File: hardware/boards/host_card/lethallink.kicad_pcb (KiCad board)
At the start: 6 copper layers, 121.2 x 98.4 mm, 198 parts, among them J1 PCIe-x4, J2 USB3_Micro_B_Amphenol, J3 Conn_02x05_Odd_Even, J4 Conn_02x04_Odd_Even, J5 Conn_02x04_Odd_Even, J6 SODIMM_260, Q1 Q_NMOS_GSD, Q2 Q_NMOS_GSD, Q3 Q_NMOS_GSD, Q4 Q_NMOS_GSD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

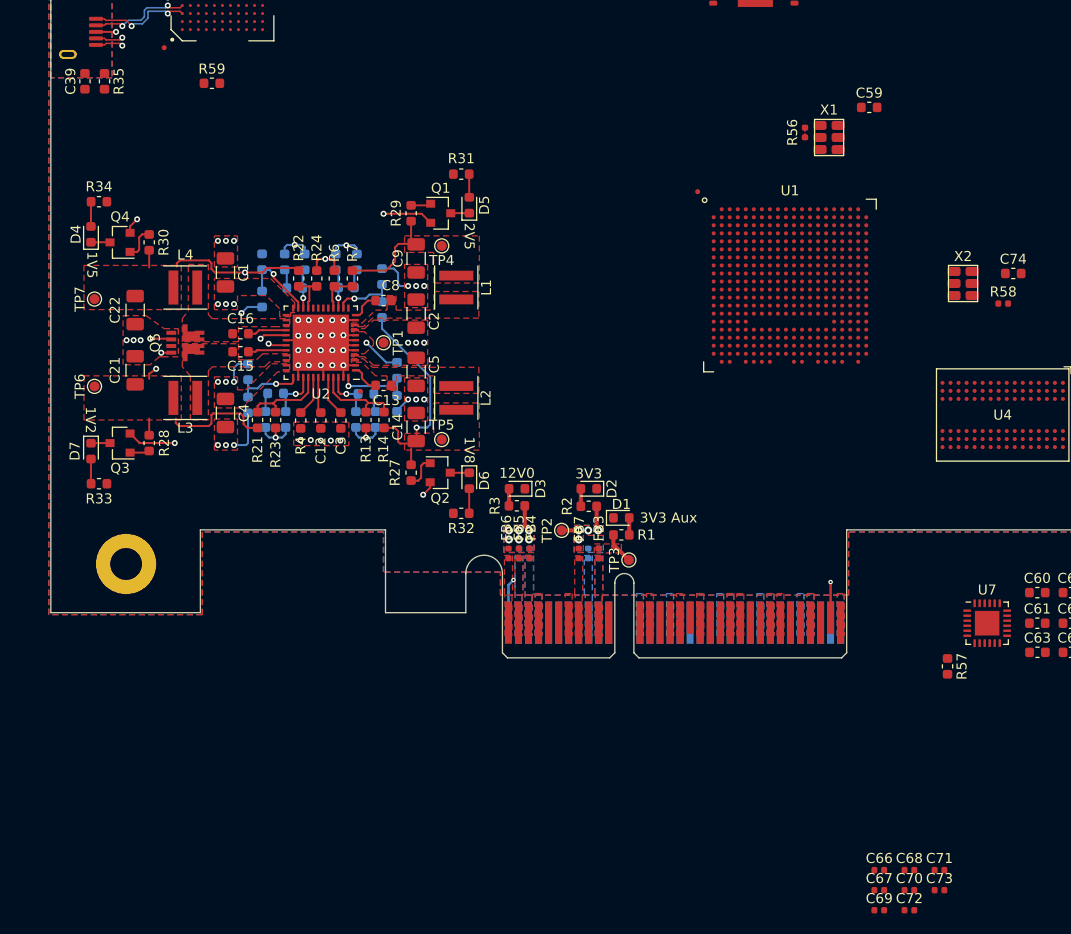
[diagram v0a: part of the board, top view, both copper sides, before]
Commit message: Routed the PCIe TX and RX lines + wiggles, activly routing the clock
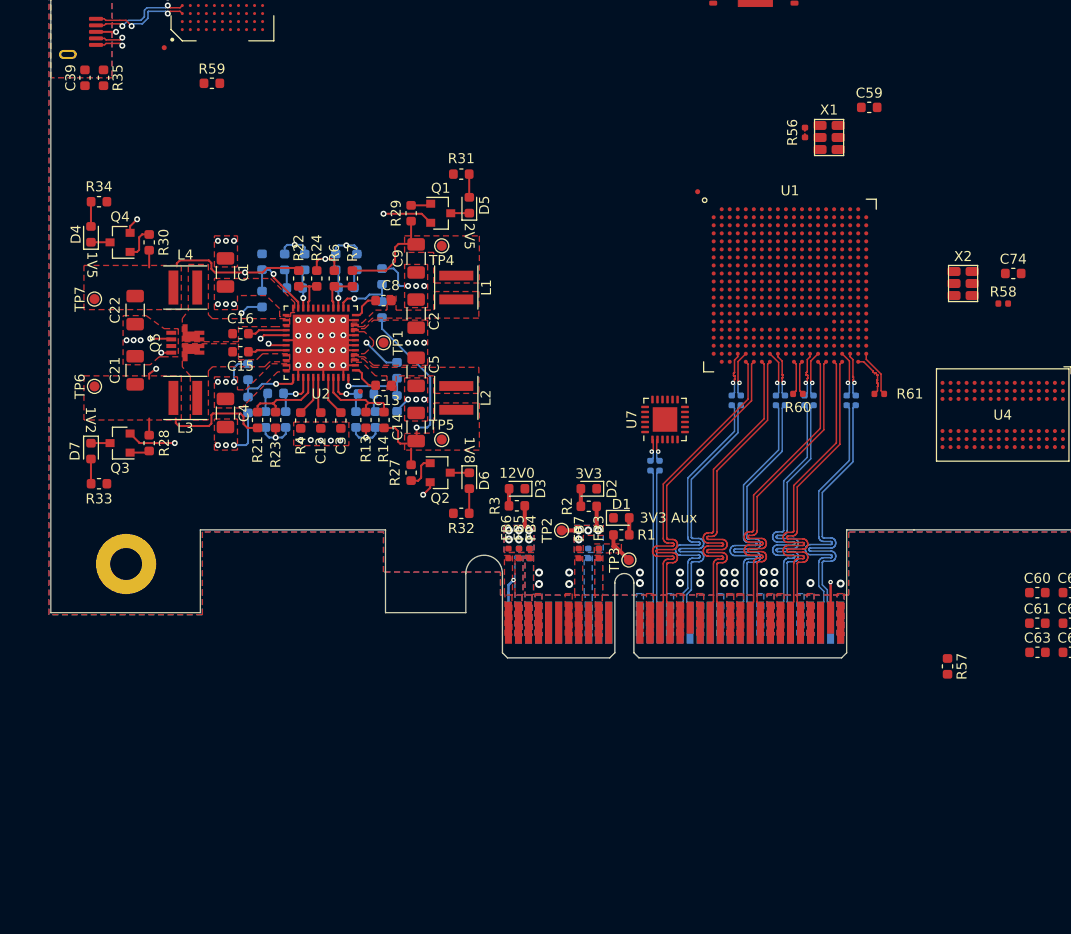
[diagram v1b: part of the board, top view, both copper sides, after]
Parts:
- added C75: 0.1uF, Capacitor_SMD:C_0402_1005Metric, B.Cu at (78.1, 107.7)
- added C76: 0.1uF, Capacitor_SMD:C_0402_1005Metric, B.Cu at (77.2, 107.7)
- added R60: 100, Resistor_SMD:R_0402_1005Metric, F.Cu at (91.9, 100.5)
- added R61: 100, Resistor_SMD:R_0402_1005Metric, F.Cu at (100.0, 100.5)
- C66, C67, C68, C69, C70, C71, C72, C73: value 100nF -> 0.1uF; moved to B.Cu
- moved C73 51.5 mm to (89.7, 101.2), turned to 90 degrees
- moved C69 51.2 mm to (93.5, 101.2), turned to 90 degrees
- moved C72 51.2 mm to (96.8, 101.2), turned to 90 degrees
- moved C68 49.7 mm to (86.2, 101.2), turned to 90 degrees
- moved C67 49.4 mm to (92.5, 101.2), turned to 90 degrees
- moved C71 49.3 mm to (90.6, 101.2), turned to 90 degrees
- moved C70 49.1 mm to (97.7, 101.2), turned to 90 degrees
- moved C66 49.1 mm to (85.3, 101.2), turned to 90 degrees
- moved U7 38.0 mm to (78.7, 103.1), turned to 90 degrees
- moved R35 0.36 mm to (22.7, 69.0)
- moved C39 0.35 mm to (20.9, 69.0)
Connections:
- J1 pad B19: /PCIe Interface/TX1_N -> /PCIe Interface/TX1_P
- U1 pad Y16: /PCIe Interface/TX3_N -> /PCIe Interface/TX3_P
- U1 pad Y17: /PCIe Interface/TX3_P -> /PCIe Interface/TX3_N
- U1 pad Y7: /PCIe Interface/TX1_N -> /PCIe Interface/TX1_P
- U7 pad 1: /PCIe Interface/REFCLK_P -> /PCIe Interface/REFCLK+
- U7 pad 10: Net-(U7-Pad10) -> /PCIe Interface/REFCLK1+
- U7 pad 13: Net-(U7-Pad13) -> /PCIe Interface/REFCLK0-
- U7 pad 14: Net-(U7-Pad14) -> /PCIe Interface/REFCLK0+
- U7 pad 17: /PCIe Interface/REFCLK1- -> Net-(U7-Pad17)
- U7 pad 18: /PCIe Interface/REFCLK1+ -> Net-(U7-Pad18)
- U7 pad 2: /PCIe Interface/REFCLK_N -> /PCIe Interface/REFCLK-
- U7 pad 21: /PCIe Interface/REFCLK0- -> Net-(U7-Pad21)
- U7 pad 22: /PCIe Interface/REFCLK0+ -> Net-(U7-Pad22)
- U7 pad 9: Net-(U7-Pad9) -> /PCIe Interface/REFCLK1-
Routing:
- net /PCIe Interface/TX1_P: track 0.00 -> 35.0 mm
- net /PCIe Interface/TX1_N: track 0.00 -> 35.0 mm
- net /PCIe Interface/TX2_P: track 0.00 -> 35.0 mm
- net /PCIe Interface/TX2_N: track 0.00 -> 35.0 mm
- net /PCIe Interface/TX3_P: track 0.00 -> 35.0 mm
- net /PCIe Interface/TX3_N: track 0.00 -> 35.0 mm
- net /PCIe Interface/TX0_P: track 0.00 -> 35.0 mm
- net /PCIe Interface/TX0_N: track 0.00 -> 35.0 mm
- net /PCIe Interface/RX2_P: track 0.00 -> 30.3 mm
- net /PCIe Interface/RX2_N: track 0.00 -> 30.3 mm
- net /PCIe Interface/RX3_P: track 0.00 -> 30.3 mm
- net /PCIe Interface/RX3_N: track 0.00 -> 30.3 mm
- net /PCIe Interface/RX0_P: track 0.00 -> 30.3 mm
- net /PCIe Interface/RX0_N: track 0.00 -> 30.3 mm
- net /PCIe Interface/RX1_P: track 0.00 -> 30.2 mm
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
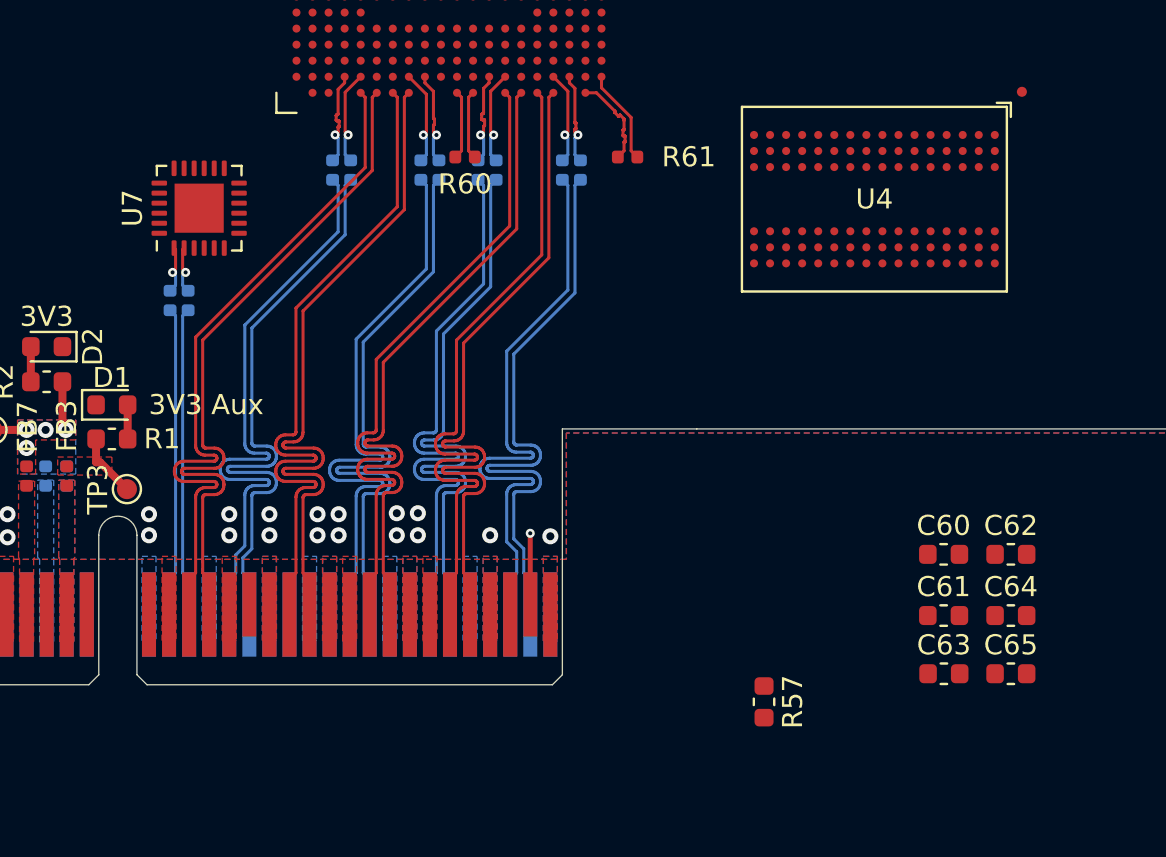
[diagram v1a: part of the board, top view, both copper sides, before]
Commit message: Completed the layout for the PCIe REFCLK buffer and ensured the REFCLK traces were not skewed and that they are wiggled properly
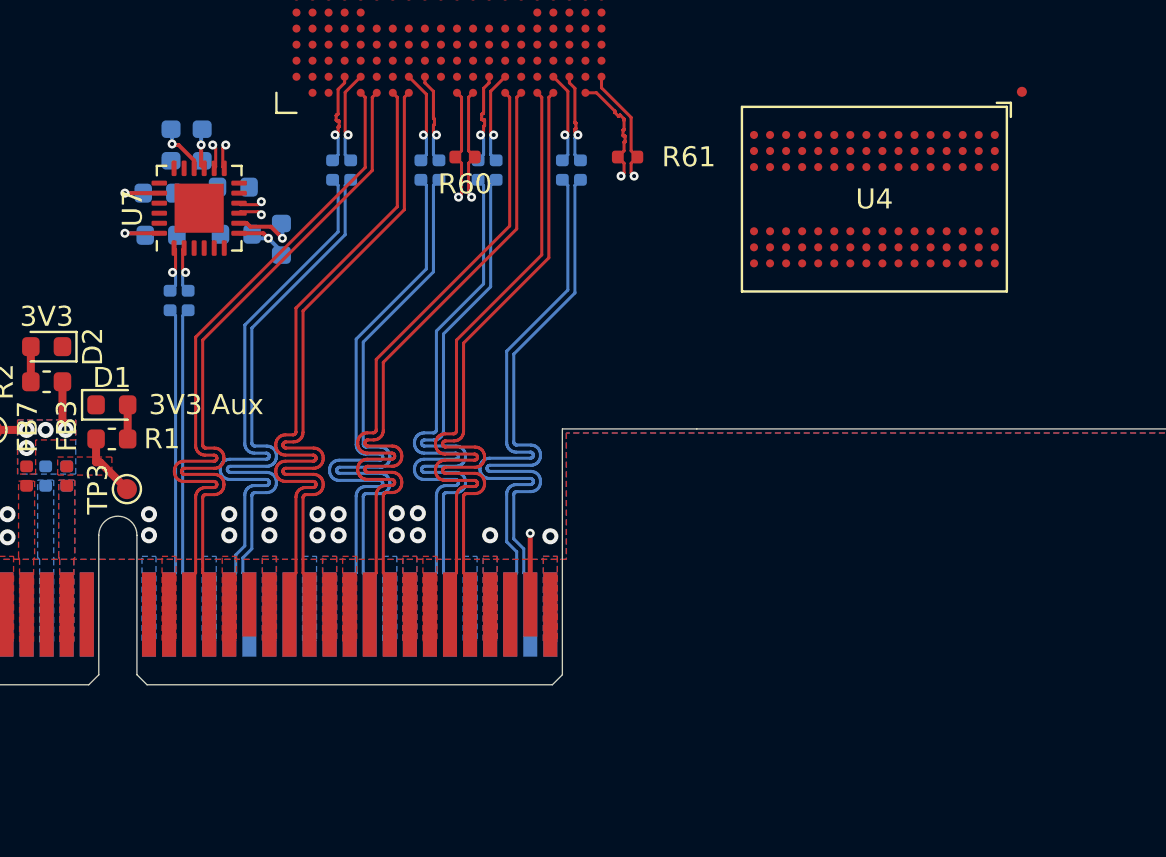
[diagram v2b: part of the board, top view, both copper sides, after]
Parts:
- C60, C61, C62, C63, C64, C65, R57: moved to B.Cu
- moved C65 48.7 mm to (76.7, 102.3), turned to 180 degrees
- moved C63 46.7 mm to (77.2, 100.0), turned to 90 degrees
- moved C64 46.6 mm to (78.8, 100.0), turned to 90 degrees
- moved C61 43.4 mm to (76.8, 104.5)
- moved C62 41.8 mm to (80.5, 104.4)
- moved C60 39.9 mm to (80.3, 102.0), turned to 180 degrees
- moved R57 33.3 mm to (82.8, 104.7)
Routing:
- net /PCIe Interface/REFCLK1+: track 4.72 -> 34.7 mm, vias 0 -> 2
- net /PCIe Interface/REFCLK1-: track 4.74 -> 34.7 mm, vias 0 -> 2
- net /PCIe Interface/REFCLK0+: track 3.42 -> 33.4 mm, vias 0 -> 2
- net /PCIe Interface/REFCLK0-: track 3.42 -> 33.4 mm, vias 0 -> 2
- net +1V8: track 20.0 -> 33.5 mm, vias 1 -> 6
- net Net-(R57-Pad1): track 0.00 -> 3.24 mm, vias 0 -> 1

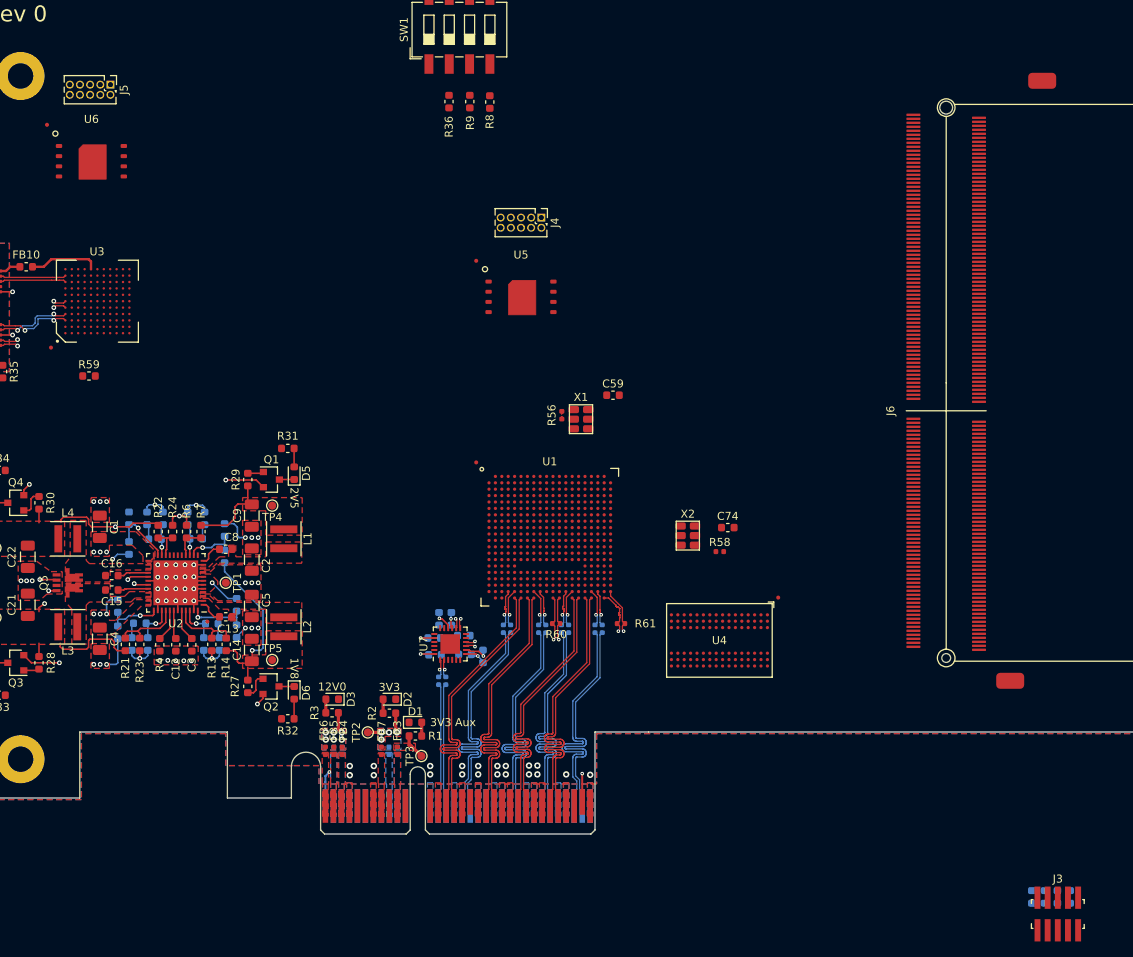
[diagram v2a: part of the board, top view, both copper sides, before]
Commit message: Added a fiducial to for U7. Changed the two pin-headers to the keyd  samtec connectors. Some other misc updates
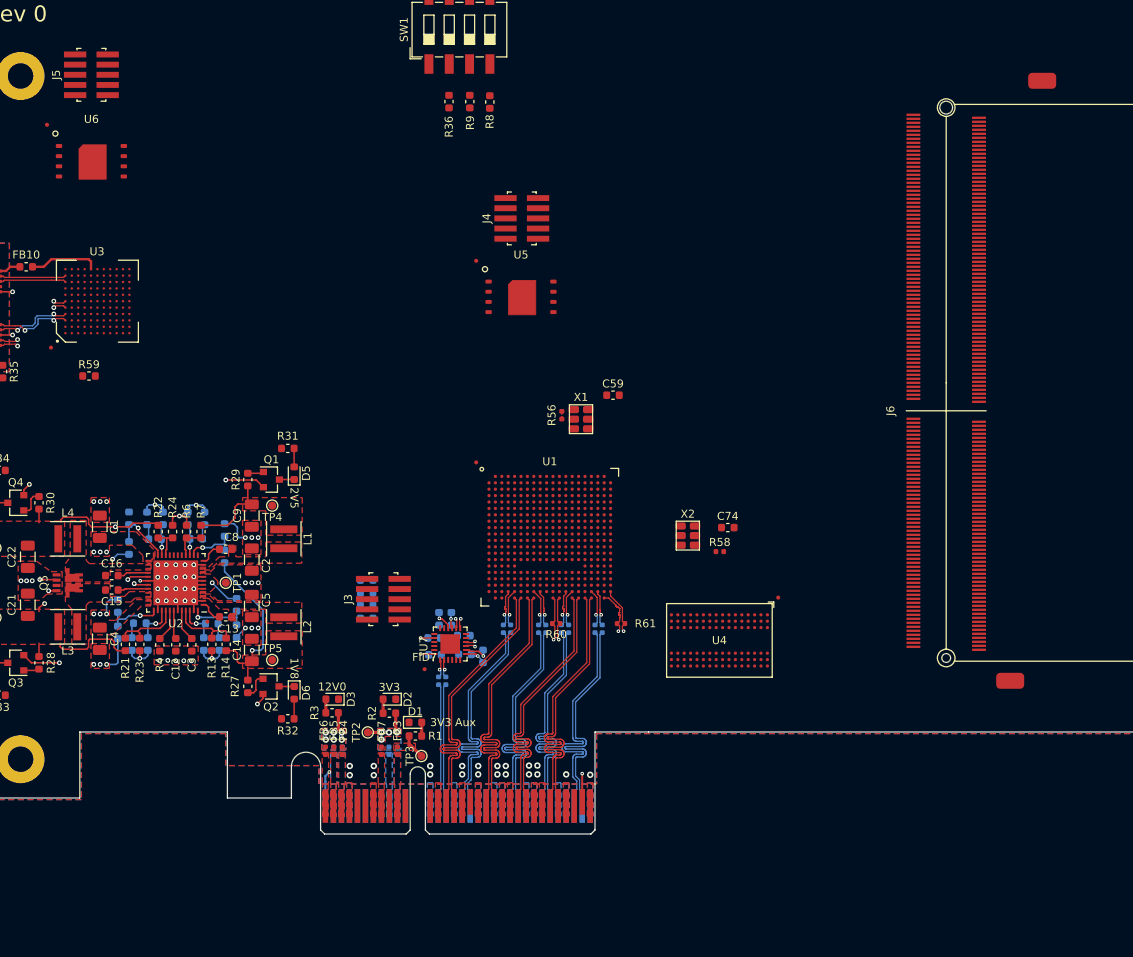
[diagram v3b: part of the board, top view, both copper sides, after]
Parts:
- added FID7: Fiducial, Fiducial:Fiducial_0.5mm_Mask1mm, F.Cu at (75.5, 106.2)
- J4, J5: footprint Connector_PinHeader_1.27mm:PinHeader_2x05_P1.27mm_Vertical -> lethalbit-connectors:FTSH-105-01-L-DV-K-TR
- moved R41 96.4 mm to (68.2, 95.1), turned to 0 degrees
- moved R40 94.3 mm to (68.2, 96.7), turned to 0 degrees
- moved J3 93.0 mm to (70.3, 97.5), turned to 90 degrees
- moved R39 92.2 mm to (68.2, 98.3), turned to 0 degrees
- moved R38 90.1 mm to (68.2, 99.9), turned to 0 degrees
- moved J5 2.68 mm to (33.8, 31.9), turned to 90 degrees
- moved J4 2.44 mm to (87.6, 49.9), turned to 90 degrees
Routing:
- net GND: track 59.5 -> 60.5 mm, vias 71 -> 72

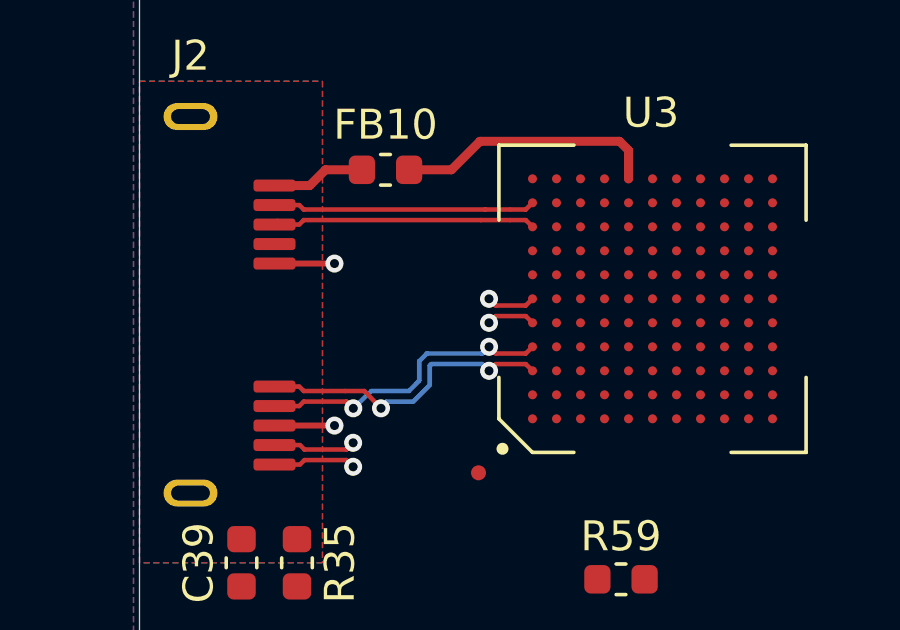
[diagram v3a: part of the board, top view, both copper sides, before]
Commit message: Fixed up the consistancy of value naming, 100nF -> 0.1uF. Added the caps for the USB SSRX lines, moved the Ferrite for VBUS to fix a net naming issue
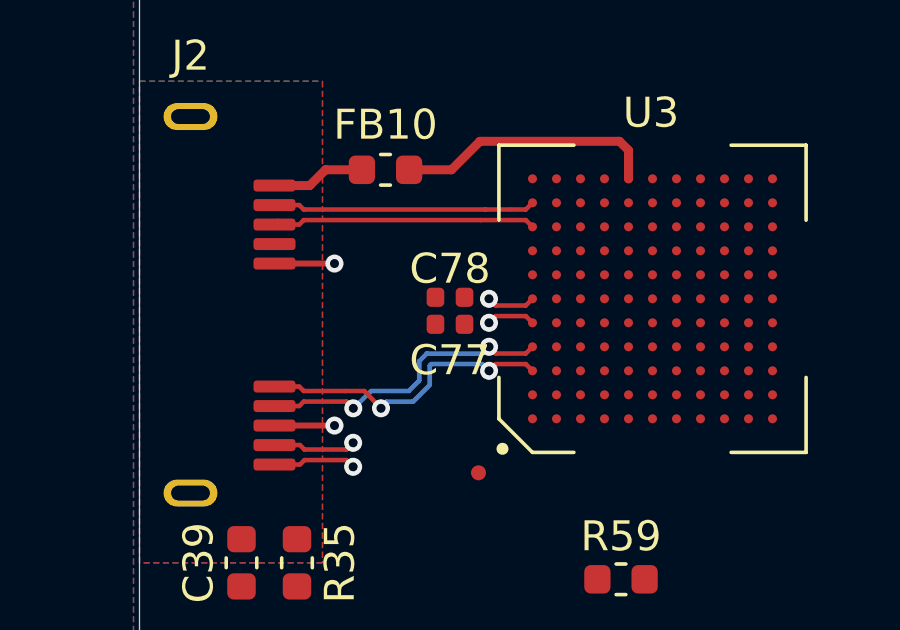
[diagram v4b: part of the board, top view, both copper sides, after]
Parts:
- added C77: 0.1uF, Capacitor_SMD:C_0402_1005Metric, F.Cu at (27.8, 61.1)
- added C78: 0.1uF, Capacitor_SMD:C_0402_1005Metric, F.Cu at (27.8, 60.2)
- C28, C29, C30, C31, C32, C34, C36, C41, C48, C51: value 100nF -> 0.1uF
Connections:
- FB10 pad 1: /USB3 Interface/VBUS -> Net-(FB10-Pad1)
- J2 pad 1: /USB3 Interface/VBUS -> /IC Power/VBUS
- U3 pad A5: /USB3 Interface/SSTX+ -> Net-(C77-Pad1)
- U3 pad A6: /USB3 Interface/SSTX- -> Net-(C78-Pad1)
- U3 pad E10: /IC Power/VBUS -> Net-(FB10-Pad1)
- U3 pad E11: /IC Power/VBUS -> Net-(FB10-Pad1)
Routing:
- net Net-(FB10-Pad1): track 0.00 -> 8.78 mm
- net /IC Power/VBUS: track 8.78 -> 3.07 mm
- net /USB3 Interface/VBUS: track 3.07 -> 0.00 mm

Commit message: Messing with the settings to try to allow for the minimal ammount of DRC violations needed to escape the large BGA package
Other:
- net class BGA Escape added: clearance 0.127, trace_width 0.127, via_dia 0.41, via_drill 0.2
- rule via_min_size: 0.45 -> 0.4
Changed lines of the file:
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@@
   )
   (setup
-    (last_trace_width 0.3)
+    (last_trace_width 0.127)
     (user_trace_width 0.127)
     (user_trace_width 0.1524)
@@
     (via_size 0.8)
     (via_drill 0.4)
-    (via_min_size 0.45)
+    (via_min_size 0.4)
     (via_min_drill 0.2)
+    (user_via 0.41 0.2)
     (user_via 0.45 0.2)
     (user_via 0.6 0.3)
-    (blind_buried_vias_allowed yes)
     (uvia_size 0.3)
     (uvia_drill 0.1)
@@
     (add_net "Net-(X2-Pad2)")
   )
+  (net_class "BGA Escape" ""
+    (clearance 0.127)
+    (trace_width 0.127)
+    (via_dia 0.41)
+    (via_drill 0.2)
+    (uvia_dia 0.3)
+    (uvia_drill 0.1)
+    (diff_pair_width 0.152)
+    (diff_pair_gap 0.2)
+  )
   (module Capacitor_SMD:C_0402_1005Metric (layer F.Cu)
